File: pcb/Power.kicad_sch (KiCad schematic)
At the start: 88 parts, among them J5 Barrel_Jack_Switch, Q2 ZXMC3A16DN8, U1 LFE5U-85F-6BG381, U8 LTC4360-2, U9 LTM8051

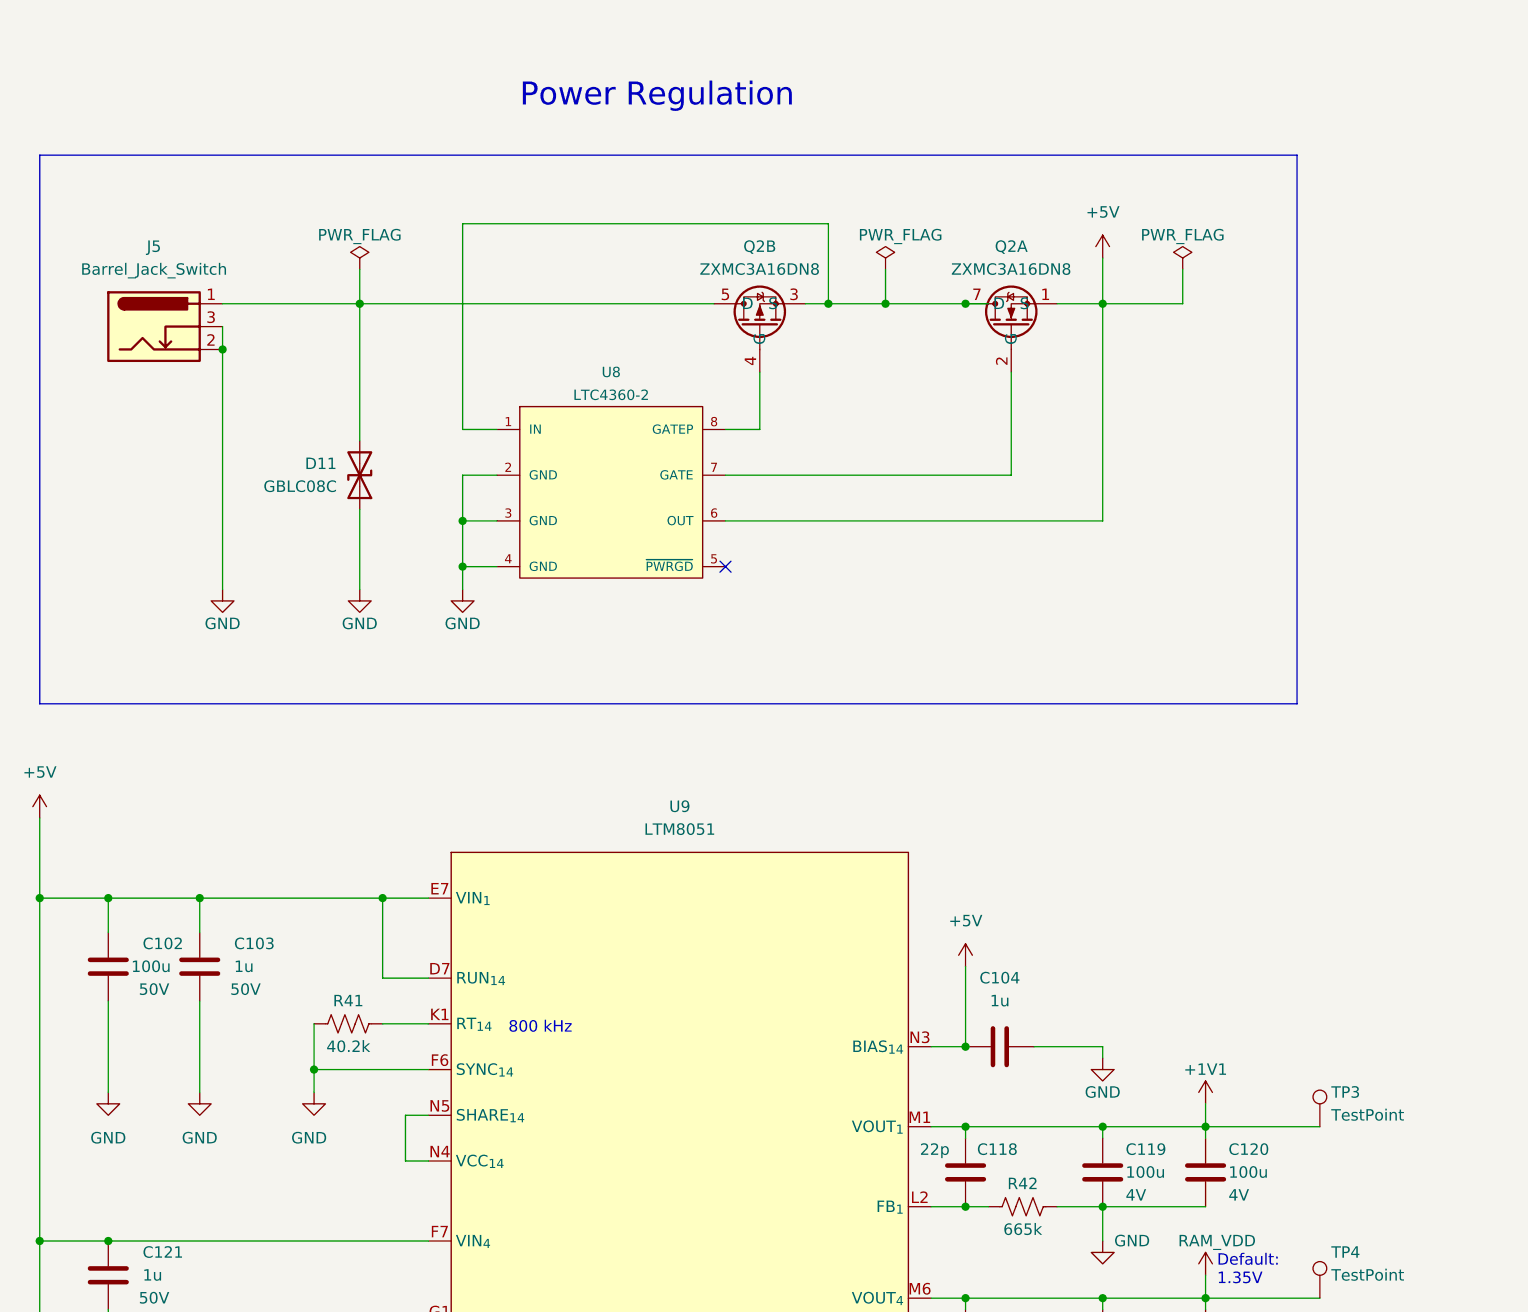
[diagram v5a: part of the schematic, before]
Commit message: Most of power routing
- Will need to retune the lengths again as final step, but only after
power is complete
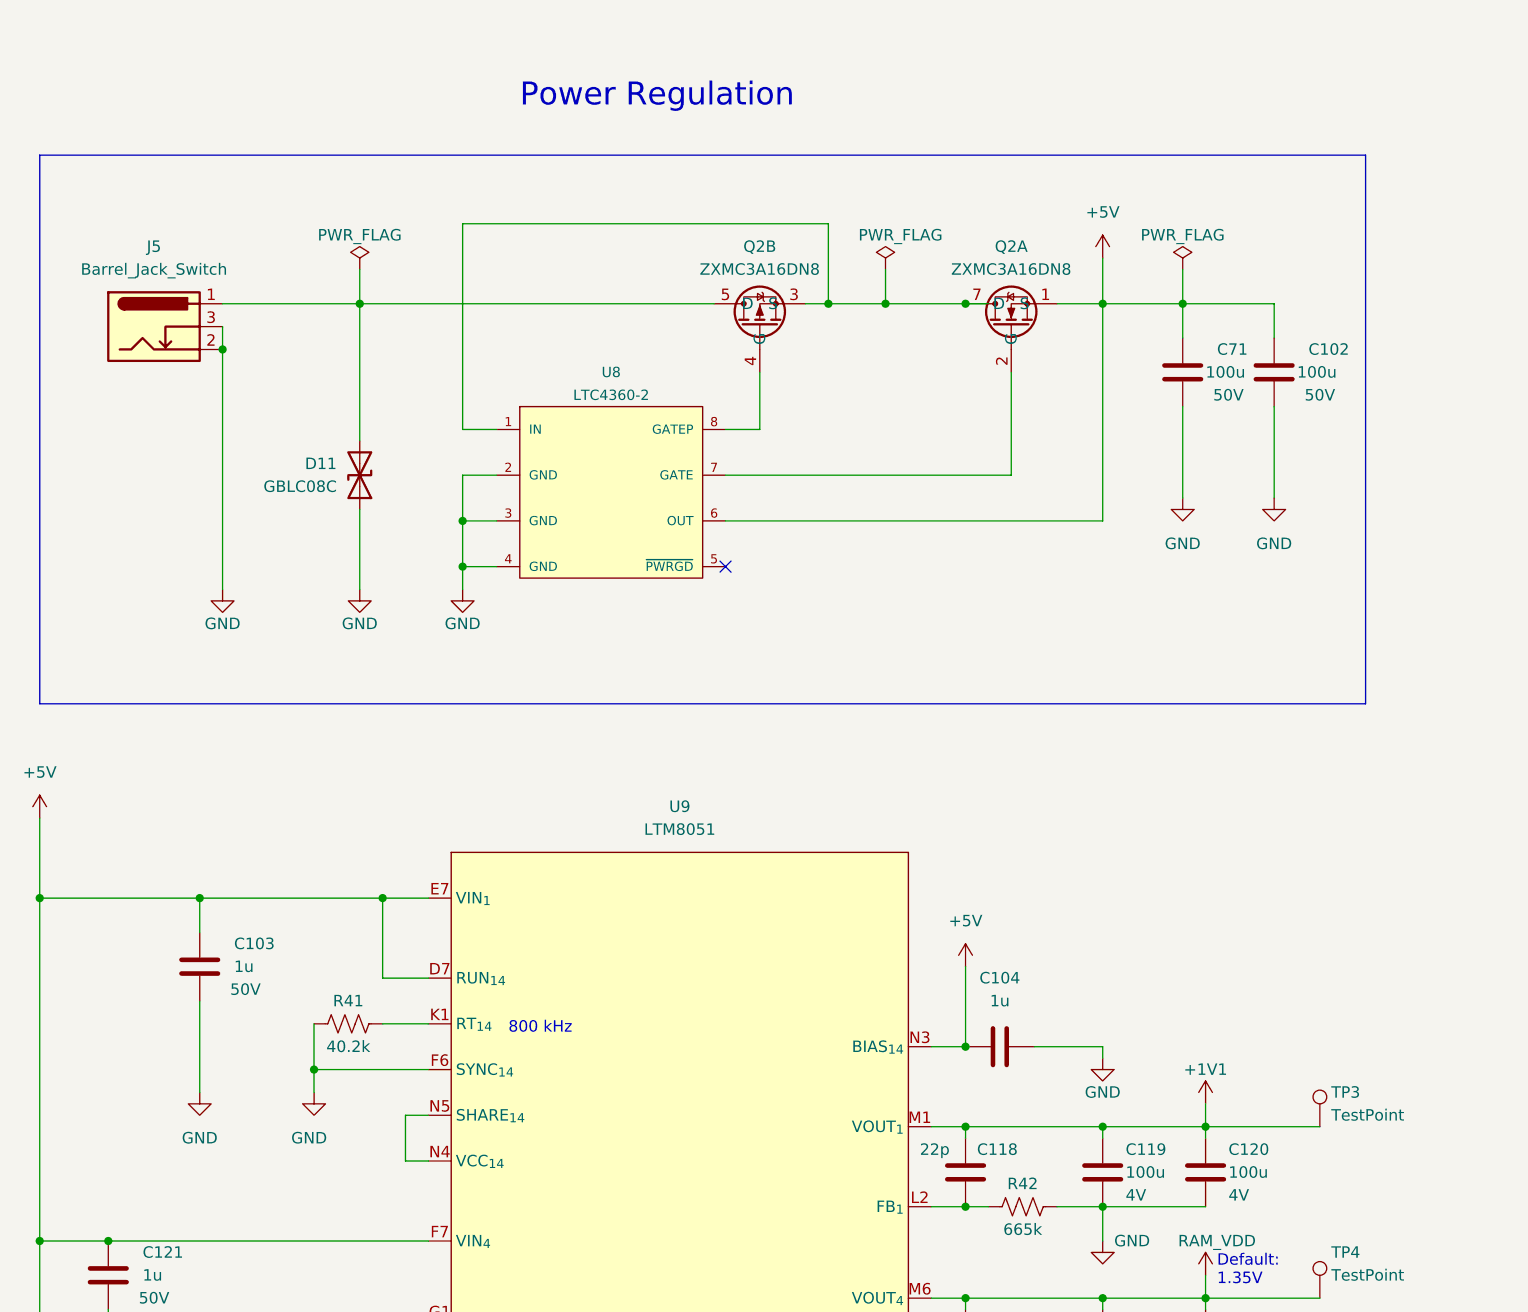
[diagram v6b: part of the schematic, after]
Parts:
- added C71: 100u, Capacitor_Tantalum_SMD:CP_EIA-6032-15_Kemet-U_Pad2.25x2.35mm_HandSolder, symbol Device:C
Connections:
- net +5V: now also C71.1
- net GND: now also C71.2
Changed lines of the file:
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@@
   (junction (at 312.42 99.06) (diameter 0) (color 0 0 0 0)
   )
-  (junction (at 48.26 111.76) (diameter 0) (color 0 0 0 0)
-  )
   (junction (at 87.63 74.93) (diameter 0) (color 0 0 0 0)
   )
@@
   )
   (junction (at 76.2 45.72) (diameter 0) (color 0 0 0 0)
+  )
+  (junction (at 167.64 45.72) (diameter 0) (color 0 0 0 0)
   )
   (junction (at 288.29 52.07) (diameter 0) (color 0 0 0 0)
@@
     (stroke (width 0) (type default) (color 0 0 0 0))
   )
-  (wire (pts (xy 48.26 111.76) (xy 58.42 111.76))
-    (stroke (width 0) (type default) (color 0 0 0 0))
-  )
   (wire (pts (xy 287.02 132.08) (xy 293.37 132.08))
     (stroke (width 0) (type default) (color 0 0 0 0))
@@
     (stroke (width 0) (type default) (color 0 0 0 0))
   )
-  (wire (pts (xy 40.64 111.76) (xy 48.26 111.76))
+  (wire (pts (xy 40.64 111.76) (xy 58.42 111.76))
     (stroke (width 0) (type default) (color 0 0 0 0))
   )
@@
     (stroke (width 0) (type default) (color 0 0 0 0))
   )
-  (wire (pts (xy 48.26 111.76) (xy 48.26 115.57))
-    (stroke (width 0) (type default) (color 0 0 0 0))
-  )
   (wire (pts (xy 334.01 132.08) (xy 340.36 132.08))
     (stroke (width 0) (type default) (color 0 0 0 0))
@@
     (stroke (width 0) (type default) (color 0 0 0 0))
   )
+  (wire (pts (xy 167.64 57.15) (xy 167.64 67.31))
+    (stroke (width 0) (type default) (color 0 0 0 0))
+  )
   (wire (pts (xy 312.42 106.68) (xy 318.77 106.68))
     (stroke (width 0) (type default) (color 0 0 0 0))
@@
     (stroke (width 0) (type default) (color 0 0 0 0))
   )
-  (polyline (pts (xy 180.34 90.17) (xy 40.64 90.17))
+  (polyline (pts (xy 187.96 90.17) (xy 40.64 90.17))
     (stroke (width 0) (type default) (color 0 0 0 0))
   )
@@
     (stroke (width 0) (type default) (color 0 0 0 0))
   )
+  (wire (pts (xy 177.8 57.15) (xy 177.8 67.31))
+    (stroke (width 0) (type default) (color 0 0 0 0))
+  )
   (wire (pts (xy 153.67 199.39) (xy 158.75 199.39))
     (stroke (width 0) (type default) (color 0 0 0 0))
@@
     (stroke (width 0) (type default) (color 0 0 0 0))
   )
-  (wire (pts (xy 48.26 123.19) (xy 48.26 133.35))
-    (stroke (width 0) (type default) (color 0 0 0 0))
-  )
   (wire (pts (xy 80.01 187.96) (xy 83.82 187.96))
     (stroke (width 0) (type default) (color 0 0 0 0))
@@
     (stroke (width 0) (type default) (color 0 0 0 0))
   )
+  (wire (pts (xy 167.64 45.72) (xy 167.64 49.53))
+    (stroke (width 0) (type default) (color 0 0 0 0))
+  )
   (wire (pts (xy 71.12 130.81) (xy 83.82 130.81))
     (stroke (width 0) (type default) (color 0 0 0 0))
@@
     (stroke (width 0) (type default) (color 0 0 0 0))
   )
-  (polyline (pts (xy 180.34 29.21) (xy 180.34 90.17))
+  (polyline (pts (xy 187.96 29.21) (xy 187.96 90.17))
     (stroke (width 0) (type default) (color 0 0 0 0))
   )
@@
     (stroke (width 0) (type default) (color 0 0 0 0))
   )
-  (polyline (pts (xy 40.64 29.21) (xy 180.34 29.21))
+  (polyline (pts (xy 40.64 29.21) (xy 187.96 29.21))
     (stroke (width 0) (type default) (color 0 0 0 0))
   )
@@
     (stroke (width 0) (type default) (color 0 0 0 0))
   )
+  (wire (pts (xy 177.8 45.72) (xy 177.8 49.53))
+    (stroke (width 0) (type default) (color 0 0 0 0))
+  )
   (wire (pts (xy 347.98 171.45) (xy 345.44 171.45))
     (stroke (width 0) (type default) (color 0 0 0 0))
@@
   )
   (wire (pts (xy 332.74 186.69) (xy 332.74 184.15))
+    (stroke (width 0) (type default) (color 0 0 0 0))
+  )
+  (wire (pts (xy 167.64 45.72) (xy 177.8 45.72))
     (stroke (width 0) (type default) (color 0 0 0 0))
   )
@@
     (pin "1")
   )
-  (symbol (lib_id "power:GND") (at 48.26 133.35 0) (unit 1)
-    (in_bom yes) (on_board yes)
-    (property "Reference" "#PWR090" (id 0) (at 48.26 139.7 0)
-      (effects (font (size 1.27 1.27)) hide)
-    )
-    (property "Value" "GND" (id 1) (at 48.26 138.43 0))
-    (property "Footprint" "" (id 2) (at 48.26 133.35 0)
-      (effects (font (size 1.27 1.27)) hide)
-    )
-    (property "Datasheet" "" (id 3) (at 48.26 133.35 0)
-      (effects (font (size 1.27 1.27)) hide)
-    )
-    (pin "1")
-  )
   (symbol (lib_id "Device:C") (at 337.82 80.01 0) (unit 1)
     (in_bom yes) (on_board yes)
@@
     (pin "2")
   )
+  (symbol (lib_id "Device:C") (at 167.64 53.34 0) (unit 1)
+    (in_bom yes) (on_board yes)
+    (property "Reference" "C71" (id 0) (at 171.45 50.8 0)
+      (effects (font (size 1.27 1.27)) (justify left))
+    )
+    (property "Value" "100u" (id 1) (at 170.18 53.34 0)
+      (effects (font (size 1.27 1.27)) (justify left))
+    )
+    (property "Footprint" "Capacitor_Tantalum_SMD:CP_EIA-6032-15_Kemet-U_Pad2.25x2.35mm_HandSolder" (id 2) (at 168.6052 57.15 0)
+      (effects (font (size 1.27 1.27)) hide)
+    )
+    (property "Datasheet" "~" (id 3) (at 167.64 53.34 0)
+      (effects (font (size 1.27 1.27)) hide)
+    )
+    (property "Voltage" "50V" (id 4) (at 172.72 55.88 0))
+    (pin "1")
+    (pin "2")
+  )
   (symbol (lib_id "Device:C") (at 353.06 128.27 0) (unit 1)
     (in_bom yes) (on_board yes)
@@
     (pin "1")
     (pin "2")
+  )
+  (symbol (lib_id "power:GND") (at 177.8 67.31 0) (unit 1)
+    (in_bom yes) (on_board yes)
+    (property "Reference" "#PWR0127" (id 0) (at 177.8 73.66 0)
+      (effects (font (size 1.27 1.27)) hide)
+    )
+    (property "Value" "GND" (id 1) (at 177.8 72.39 0))
+    (property "Footprint" "" (id 2) (at 177.8 67.31 0)
+      (effects (font (size 1.27 1.27)) hide)
+    )
+    (property "Datasheet" "" (id 3) (at 177.8 67.31 0)
+      (effects (font (size 1.27 1.27)) hide)
+    )
+    (pin "1")
   )
   (symbol (lib_id "Device:C") (at 238.76 80.01 0) (unit 1)
@@
       (effects (font (size 1.27 1.27)) hide)
     )
-    (pin "1")
-    (pin "2")
-  )
-  (symbol (lib_id "Device:C") (at 48.26 119.38 0) (unit 1)
-    (in_bom yes) (on_board yes)
-    (property "Reference" "C102" (id 0) (at 52.07 116.84 0)
-      (effects (font (size 1.27 1.27)) (justify left))
-    )
-    (property "Value" "100u" (id 1) (at 50.8 119.38 0)
-      (effects (font (size 1.27 1.27)) (justify left))
-    )
-    (property "Footprint" "Capacitor_Tantalum_SMD:CP_EIA-6032-15_Kemet-U_Pad2.25x2.35mm_HandSolder" (id 2) (at 49.2252 123.19 0)
-      (effects (font (size 1.27 1.27)) hide)
-    )
-    (property "Datasheet" "~" (id 3) (at 48.26 119.38 0)
-      (effects (font (size 1.27 1.27)) hide)
-    )
-    (property "Voltage" "50V" (id 4) (at 53.34 121.92 0))
     (pin "1")
     (pin "2")
@@
     (pin "6")
   )
+  (symbol (lib_id "power:GND") (at 167.64 67.31 0) (unit 1)
+    (in_bom yes) (on_board yes)
+    (property "Reference" "#PWR090" (id 0) (at 167.64 73.66 0)
+      (effects (font (size 1.27 1.27)) hide)
+    )
+    (property "Value" "GND" (id 1) (at 167.64 72.39 0))
+    (property "Footprint" "" (id 2) (at 167.64 67.31 0)
+      (effects (font (size 1.27 1.27)) hide)
+    )
+    (property "Datasheet" "" (id 3) (at 167.64 67.31 0)
+      (effects (font (size 1.27 1.27)) hide)
+    )
+    (pin "1")
+  )
   (symbol (lib_id "Device:C") (at 238.76 128.27 0) (unit 1)
     (in_bom yes) (on_board yes)
@@
     (pin "1")
   )
+  (symbol (lib_id "Device:C") (at 177.8 53.34 0) (unit 1)
+    (in_bom yes) (on_board yes)
+    (property "Reference" "C102" (id 0) (at 181.61 50.8 0)
+      (effects (font (size 1.27 1.27)) (justify left))
+    )
+    (property "Value" "100u" (id 1) (at 180.34 53.34 0)
+      (effects (font (size 1.27 1.27)) (justify left))
+    )
+    (property "Footprint" "Capacitor_Tantalum_SMD:CP_EIA-6032-15_Kemet-U_Pad2.25x2.35mm_HandSolder" (id 2) (at 178.7652 57.15 0)
+      (effects (font (size 1.27 1.27)) hide)
+    )
+    (property "Datasheet" "~" (id 3) (at 177.8 53.34 0)
+      (effects (font (size 1.27 1.27)) hide)
+    )
+    (property "Voltage" "50V" (id 4) (at 182.88 55.88 0))
+    (pin "1")
+    (pin "2")
+  )
   (symbol (lib_id "Device:C") (at 238.76 55.88 0) (unit 1)

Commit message: Rev. A before fab comments
- Added gerbers, mount positions, etc.
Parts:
- U8: footprint Package_TO_SOT_SMD:SC-70-8 -> LTC4360_SC70
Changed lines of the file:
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@@
       (effects (font (size 1.143 1.143)))
     )
-    (property "Footprint" "Package_TO_SOT_SMD:SC-70-8" (id 2) (at 104.902 63.5 0)
+    (property "Footprint" "LTC4360_SC70" (id 2) (at 104.902 63.5 0)
       (effects (font (size 0.508 0.508)) hide)
     )

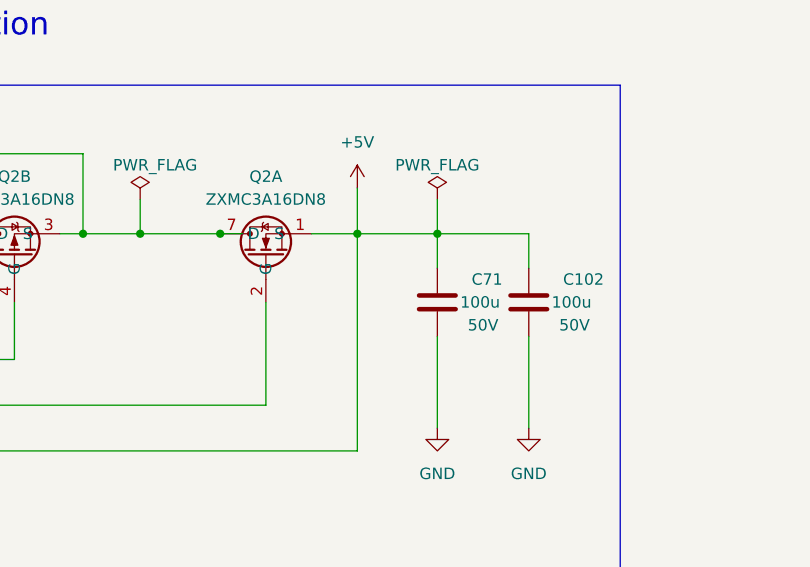
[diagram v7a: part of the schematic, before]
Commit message: Started revision B
- D8 polarity was reversed
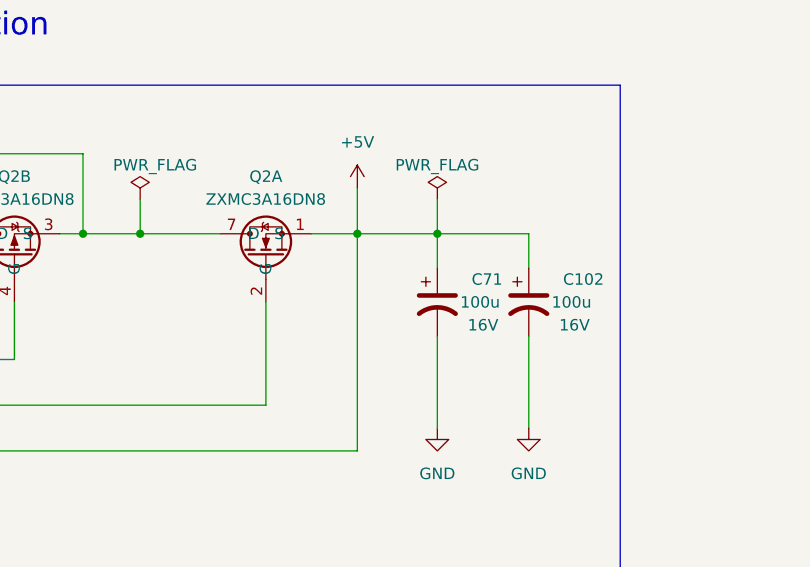
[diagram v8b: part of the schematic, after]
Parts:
- C102, C71: symbol Device:C -> Device:C_Polarized_US; Voltage 50V -> 16V
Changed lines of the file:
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@@
     (title "ECP5U85-BSE-USB Breakout Board")
     (date "2022-02-02")
-    (rev "A")
+    (rev "B")
     (company "OEPS & Open Ephys, Inc.")
     (comment 1 "Jonathan Newman")
@@
   )
   (junction (at 327.66 124.46) (diameter 0) (color 0 0 0 0)
-  )
-  (junction (at 143.51 45.72) (diameter 0) (color 0 0 0 0)
   )
   (junction (at 332.74 184.15) (diameter 0) (color 0 0 0 0)
@@
     (stroke (width 0) (type default) (color 0 0 0 0))
   )
-  (wire (pts (xy 146.05 45.72) (xy 143.51 45.72))
-    (stroke (width 0) (type default) (color 0 0 0 0))
-  )
   (wire (pts (xy 158.75 156.21) (xy 170.18 156.21))
     (stroke (width 0) (type default) (color 0 0 0 0))
@@
     (pin "2")
   )
-  (symbol (lib_id "Device:C") (at 167.64 53.34 0) (unit 1)
+  (symbol (lib_id "Device:C_Polarized_US") (at 167.64 53.34 0) (unit 1)
     (in_bom yes) (on_board yes)
     (property "Reference" "C71" (id 0) (at 171.45 50.8 0)
@@
       (effects (font (size 1.27 1.27)) (justify left))
     )
-    (property "Footprint" "Capacitor_Tantalum_SMD:CP_EIA-6032-15_Kemet-U_Pad2.25x2.35mm_HandSolder" (id 2) (at 168.6052 57.15 0)
+    (property "Footprint" "Capacitor_Tantalum_SMD:CP_EIA-6032-15_Kemet-U_Pad2.25x2.35mm_HandSolder" (id 2) (at 167.64 53.34 0)
       (effects (font (size 1.27 1.27)) hide)
     )
@@
       (effects (font (size 1.27 1.27)) hide)
     )
-    (property "Voltage" "50V" (id 4) (at 172.72 55.88 0))
+    (property "Voltage" "16V" (id 4) (at 172.72 55.88 0))
     (pin "1")
     (pin "2")
@@
     (pin "1")
   )
-  (symbol (lib_id "Device:C") (at 177.8 53.34 0) (unit 1)
+  (symbol (lib_id "Device:C_Polarized_US") (at 177.8 53.34 0) (unit 1)
     (in_bom yes) (on_board yes)
     (property "Reference" "C102" (id 0) (at 181.61 50.8 0)
@@
       (effects (font (size 1.27 1.27)) (justify left))
     )
-    (property "Footprint" "Capacitor_Tantalum_SMD:CP_EIA-6032-15_Kemet-U_Pad2.25x2.35mm_HandSolder" (id 2) (at 178.7652 57.15 0)
+    (property "Footprint" "Capacitor_Tantalum_SMD:CP_EIA-6032-15_Kemet-U_Pad2.25x2.35mm_HandSolder" (id 2) (at 177.8 53.34 0)
       (effects (font (size 1.27 1.27)) hide)
     )
@@
       (effects (font (size 1.27 1.27)) hide)
     )
-    (property "Voltage" "50V" (id 4) (at 182.88 55.88 0))
-    (pin "1")
-    (pin "2")
+    (property "Voltage" "16V" (id 4) (at 182.88 55.88 0))
+    (pin "1")
+    (pin "2")
